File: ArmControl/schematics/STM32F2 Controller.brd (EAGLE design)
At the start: 100 x 50 mm, 96 parts, among them IC1 REG1117, IC2 TL072D, IC3 TL072D, Q301 BC846, Q701 BC846, U1 STM32F10XRXT6

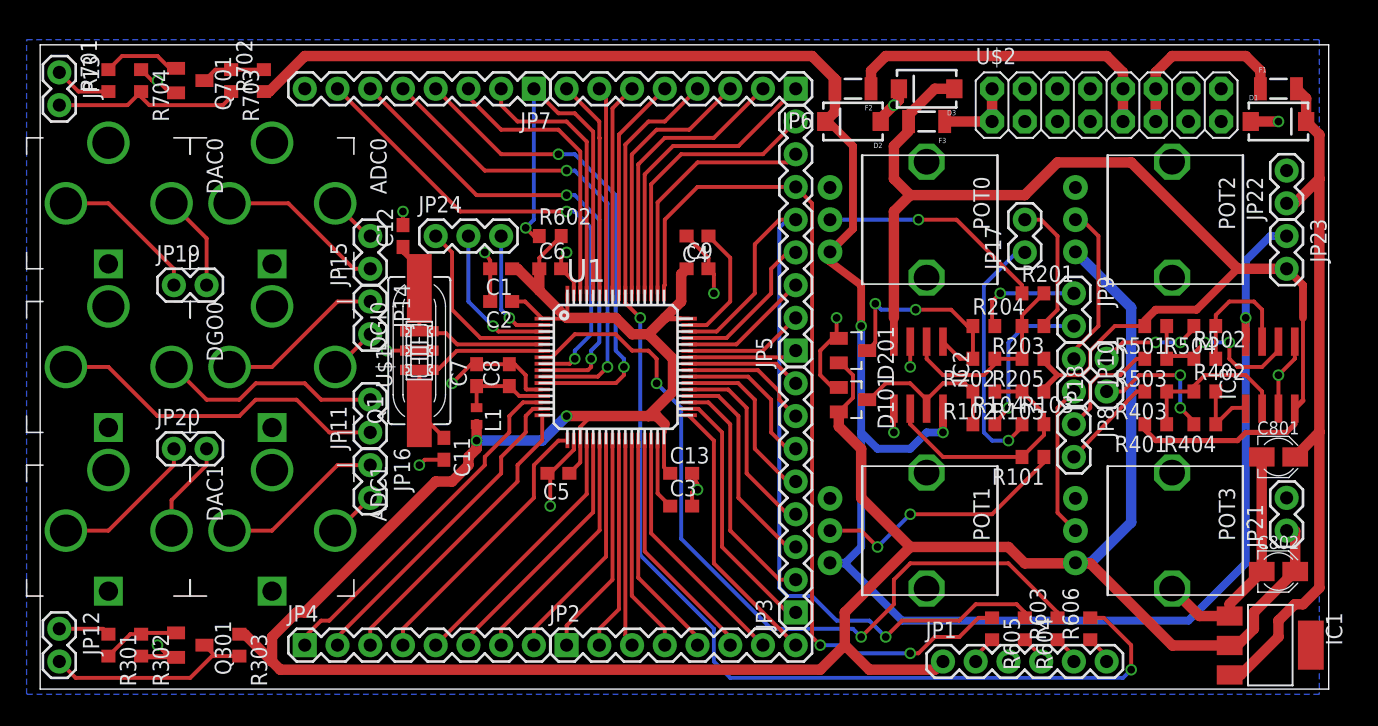
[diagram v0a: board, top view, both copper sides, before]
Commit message: added and layed out labels
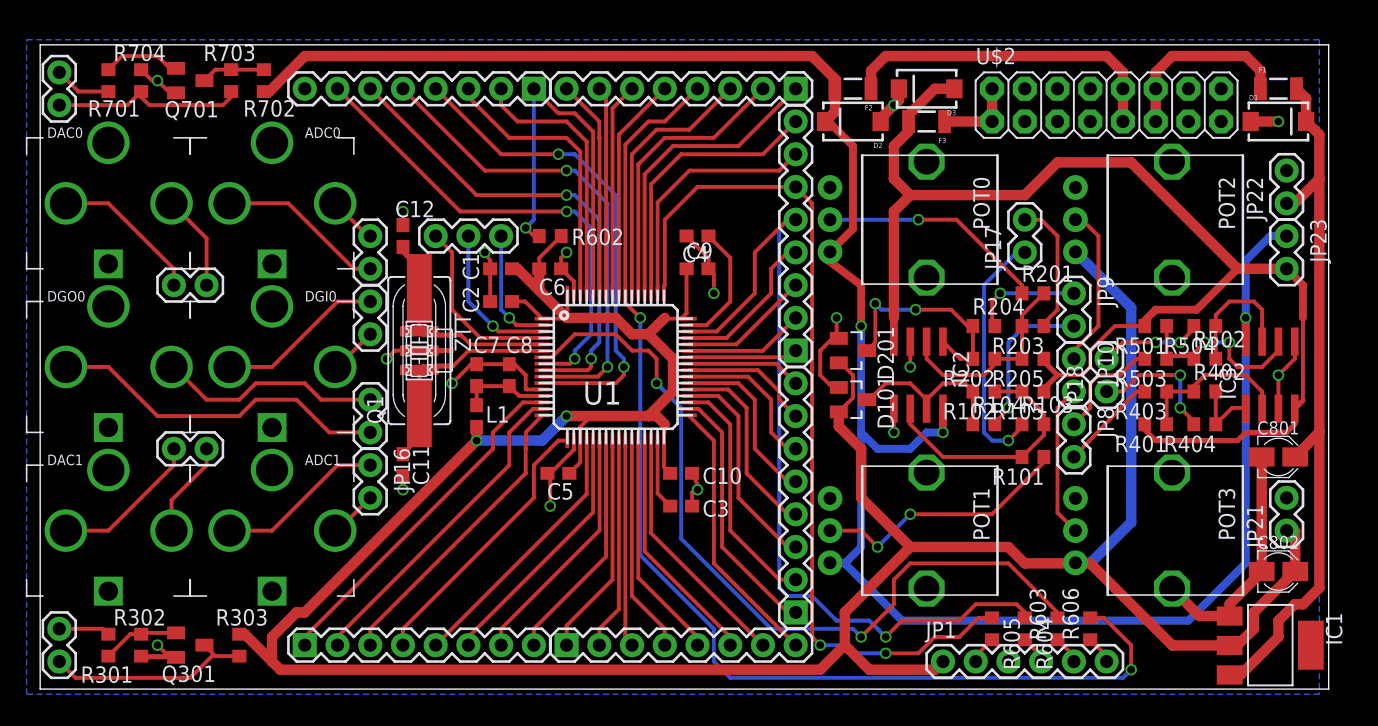
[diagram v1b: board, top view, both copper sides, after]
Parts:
- added ZTT: CERAMIC_RESONATOR, Rebel:CSTCE_G_A
- L1: value BML15HG601SN1 -> INDUCTOR; device inductors:0402 -> Rebel:0603
- moved C11 3.42 mm to (29.2, 17.8)
- renumbered C13 to C10
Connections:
- net GND: now also ZTT.P$2
- net N$19: now also ZTT.P$1
- net N$20: now also ZTT.P$3
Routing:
- net +3V3: track 252.5 -> 251.1 mm
- net N$20: track 16.2 -> 17.3 mm
- net GND: track 88.5 -> 89.3 mm

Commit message: added and layed out labels
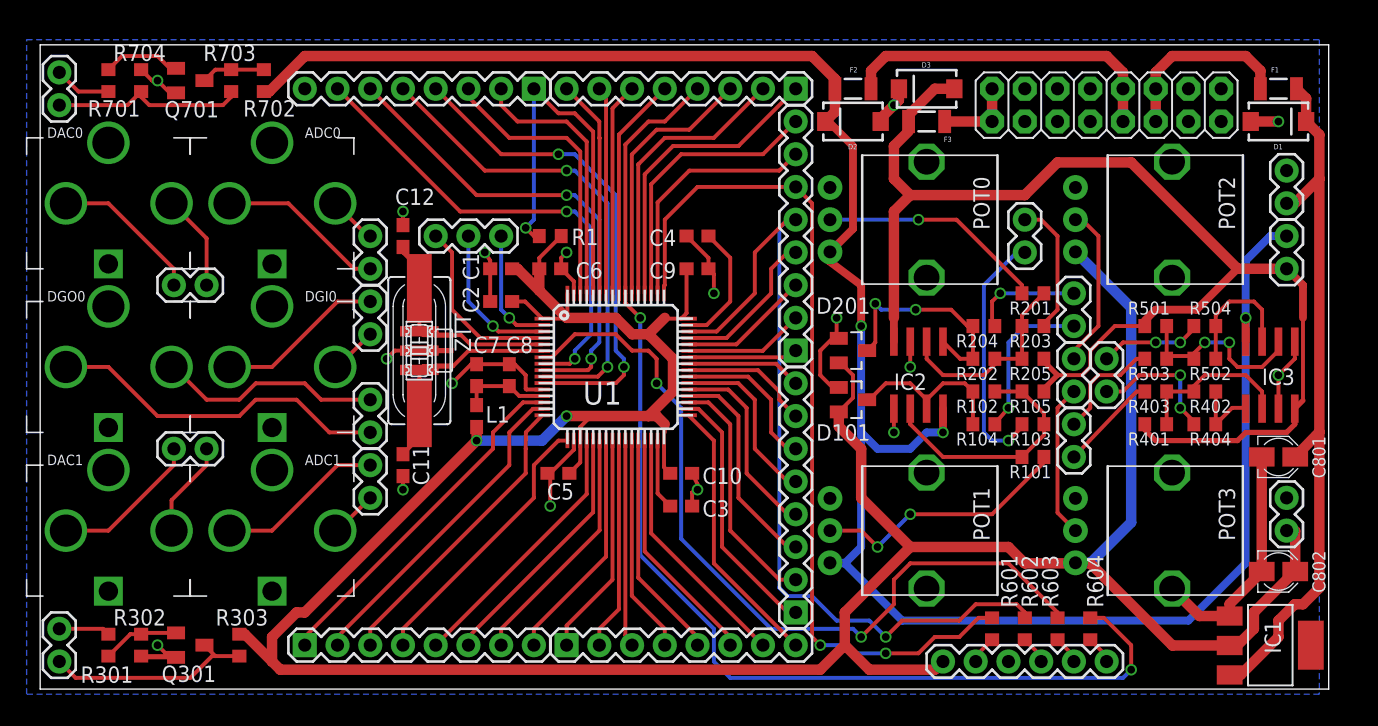
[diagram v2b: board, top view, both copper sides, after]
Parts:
- removed R606: 22R, resistor:R0603
- added R1: 10K, resistor:R0603
- R602: value 10K -> 22R
- moved R602 47.8 mm to (77.5, 5.08), turned to 270 degrees
- moved R604 5.08 mm to (82.5, 5.08), turned to 90 degrees
- renumbered R605 to R601
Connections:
- net +3V3: now also R1.2; no longer R602.2
- net BOOT0: now also R1.1; no longer R602.1
- net PA13: now also R602.1; no longer R604.1
- net PB3: now also R604.2; no longer R606.2
- net SWDIO: now also R602.2; no longer R604.2
- net SWO: now also R604.1; no longer R606.1
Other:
- board text added: "+12"
- board text added: "+5V"
- board text added: "-12"
- board text added: "3V3"
- board text added: "BOOT0"
- board text added: "Control Rev 01"
- board text added: "GND"
- board text added: "PA0"
- board text added: "PA1"
- board text added: "PA10"
- board text added: "PA11"
- board text added: "PA12"
- board text added: "PA13"
- board text added: "PA14"
- board text added: "PA15"
- board text added: "PA2"
- board text added: "PA3"
- board text added: "PA4"
- board text added: "PA5"
- board text added: "PA6"
- board text added: "PA7"
- board text added: "PA8"
- board text added: "PA9"
- board text added: "PB0"
- board text added: "PB1"
- board text added: "PB10"
- board text added: "PB11"
- board text added: "PB12"
- board text added: "PB13"
- board text added: "PB14"
- board text added: "PB15"
- board text added: "PB2"
- board text added: "PB3"
- board text added: "PB4"
- board text added: "PB5"
- board text added: "PB6"
- board text added: "PB7"
- board text added: "PB8"
- board text added: "PB9"
- board text added: "PC0"
- board text added: "PC1"
- board text added: "PC10"
- board text added: "PC11"
- board text added: "PC12"
- board text added: "PC2"
- board text added: "PC3"
- board text added: "PC4"
- board text added: "PC5"
- board text added: "PC6"
- board text added: "PC7"
- board text added: "PC8"
- board text added: "PC9"
- board text added: "PD2"
- board text added: "Rebel Technology"

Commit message: tons of old updates in one fat commit
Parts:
- added U$3: (no value), Rebel:RT-LOGO-35MM-BL
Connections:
- net N$12 renamed RST
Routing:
- net PA13: track 65.6 -> 62.3 mm
- net PB3: track 89.5 -> 88.6 mm
- net +3V3: track 251.1 -> 250.5 mm
